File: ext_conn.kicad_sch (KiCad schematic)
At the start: 8 parts, among them J1 UDPI, J2 OUT, J3 USB_C, J4 CELL

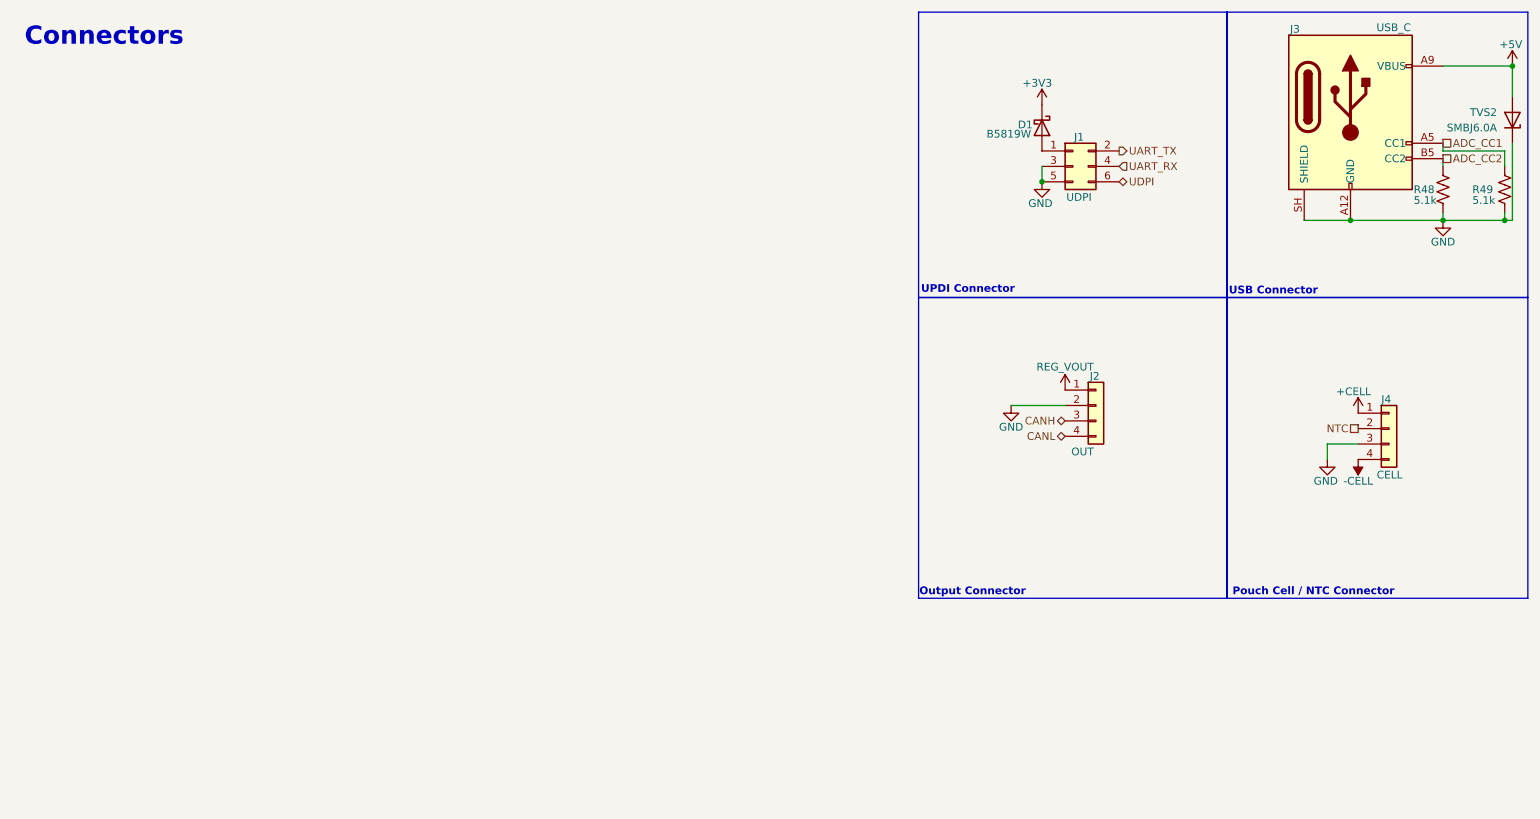
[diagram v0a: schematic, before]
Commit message: Added Graph & cleaned up title and layout
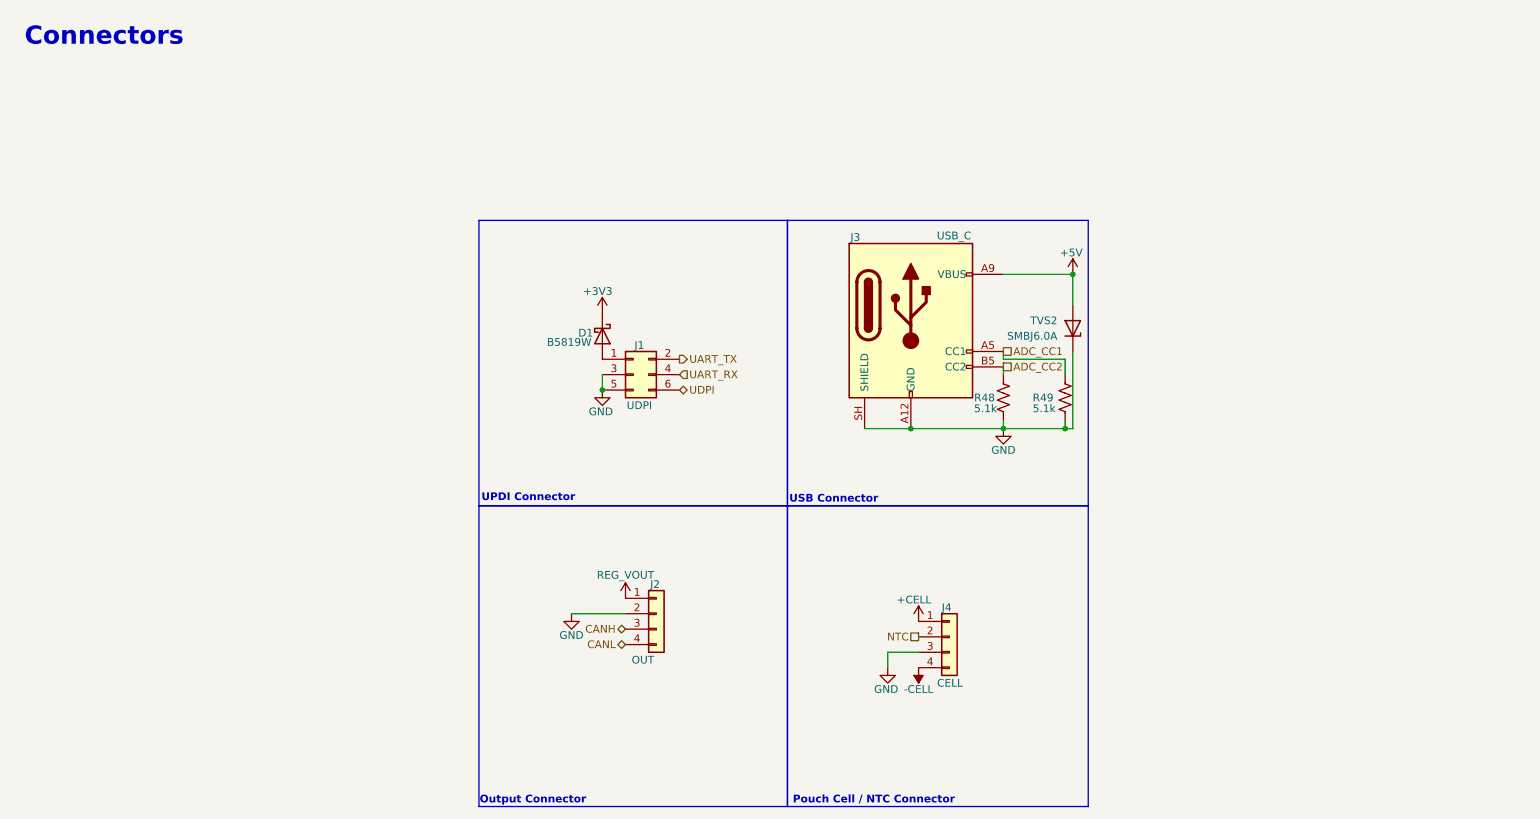
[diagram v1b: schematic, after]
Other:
- company: FETfox -> github.com/FETfox/Li-Ion_Power_Module
- title: Li Lion Power Module -> Li Lion Power Module w/ Optional Fuel Gauge &CAN Bus
- moved on the sheet: D1, J1, J2, J3, J4, R48, R49, TVS2
